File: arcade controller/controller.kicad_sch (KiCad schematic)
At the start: 21 parts, among them SW1 SW_DIP_x01, SW10 SW_DIP_x01, SW2 SW_DIP_x01, SW3 SW_DIP_x01, SW4 SW_DIP_x01, SW5 SW_DIP_x01, SW6 SW_DIP_x01, SW7 SW_DIP_x01, SW8 SW_DIP_x01, SW9 SW_DIP_x01

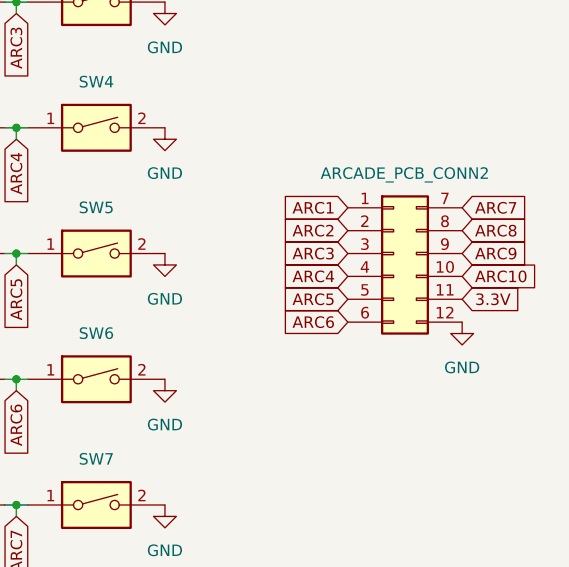
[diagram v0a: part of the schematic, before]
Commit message: updated controller with new connector
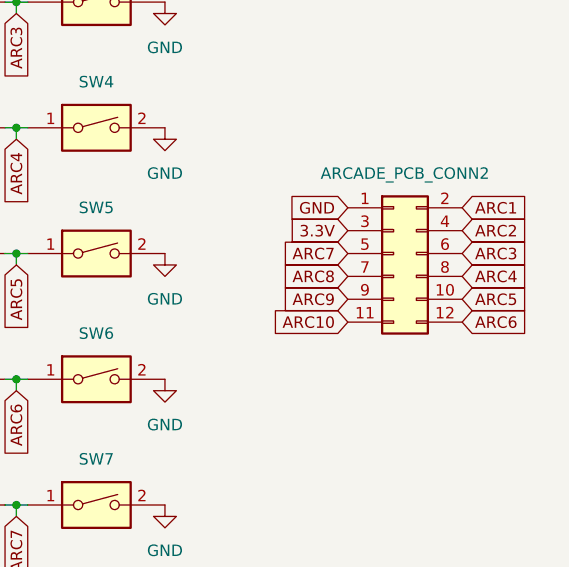
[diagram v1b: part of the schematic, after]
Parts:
- ARCADE_PCB_CONN2: value Conn_02x06_Top_Bottom -> Conn_02x06_Odd_Even; footprint Connector_Harwin:Harwin_Gecko-G125-FVX1205L0X_2x06_P1.25mm_Vertical -> Connector_PinHeader_2.54mm:PinHeader_2x06_P2.54mm_Vertical
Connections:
- net 3.3V: now also ARCADE_PCB_CONN2.3 (Pin_3); no longer ARCADE_PCB_CONN2.11 (Pin_11)
- net ARC1: now also ARCADE_PCB_CONN2.2 (Pin_2); no longer ARCADE_PCB_CONN2.1 (Pin_1)
- net ARC10: now also ARCADE_PCB_CONN2.11 (Pin_11); no longer ARCADE_PCB_CONN2.10 (Pin_10)
- net ARC2: now also ARCADE_PCB_CONN2.4 (Pin_4); no longer ARCADE_PCB_CONN2.2 (Pin_2)
- net ARC3: now also ARCADE_PCB_CONN2.6 (Pin_6); no longer ARCADE_PCB_CONN2.3 (Pin_3)
- net ARC4: now also ARCADE_PCB_CONN2.8 (Pin_8); no longer ARCADE_PCB_CONN2.4 (Pin_4)
- net ARC5: now also ARCADE_PCB_CONN2.10 (Pin_10); no longer ARCADE_PCB_CONN2.5 (Pin_5)
- net ARC6: now also ARCADE_PCB_CONN2.12 (Pin_12); no longer ARCADE_PCB_CONN2.6 (Pin_6)
- net ARC7: now also ARCADE_PCB_CONN2.5 (Pin_5); no longer ARCADE_PCB_CONN2.7 (Pin_7)
- net ARC8: now also ARCADE_PCB_CONN2.7 (Pin_7); no longer ARCADE_PCB_CONN2.8 (Pin_8)
- net GND: now also ARCADE_PCB_CONN2.1 (Pin_1); no longer ARCADE_PCB_CONN2.12 (Pin_12)

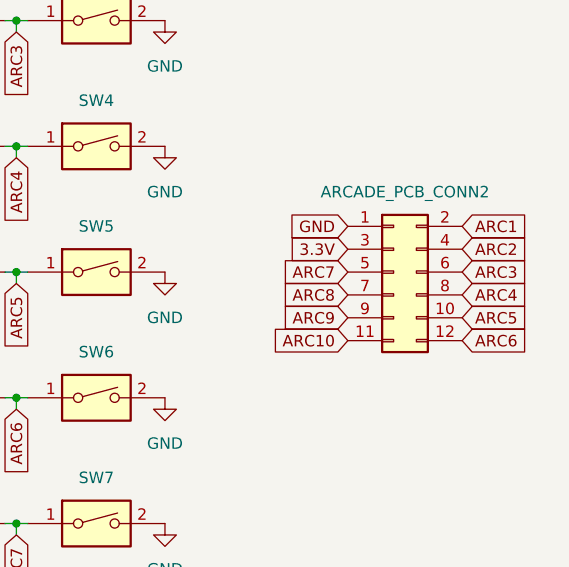
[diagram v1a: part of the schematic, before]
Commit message: update arcade controller
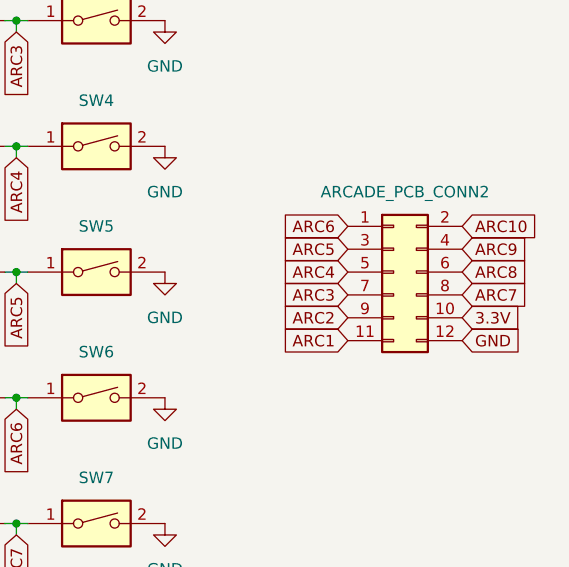
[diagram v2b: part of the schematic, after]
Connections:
- net 3.3V: now also ARCADE_PCB_CONN2.10 (Pin_10); no longer ARCADE_PCB_CONN2.3 (Pin_3)
- net ARC1: now also ARCADE_PCB_CONN2.11 (Pin_11); no longer ARCADE_PCB_CONN2.2 (Pin_2)
- net ARC10: now also ARCADE_PCB_CONN2.2 (Pin_2); no longer ARCADE_PCB_CONN2.11 (Pin_11)
- net ARC2: now also ARCADE_PCB_CONN2.9 (Pin_9); no longer ARCADE_PCB_CONN2.4 (Pin_4)
- net ARC3: now also ARCADE_PCB_CONN2.7 (Pin_7); no longer ARCADE_PCB_CONN2.6 (Pin_6)
- net ARC4: now also ARCADE_PCB_CONN2.5 (Pin_5); no longer ARCADE_PCB_CONN2.8 (Pin_8)
- net ARC5: now also ARCADE_PCB_CONN2.3 (Pin_3); no longer ARCADE_PCB_CONN2.10 (Pin_10)
- net ARC6: now also ARCADE_PCB_CONN2.1 (Pin_1); no longer ARCADE_PCB_CONN2.12 (Pin_12)
- net ARC7: now also ARCADE_PCB_CONN2.8 (Pin_8); no longer ARCADE_PCB_CONN2.5 (Pin_5)
- net ARC8: now also ARCADE_PCB_CONN2.6 (Pin_6); no longer ARCADE_PCB_CONN2.7 (Pin_7)
- net ARC9: now also ARCADE_PCB_CONN2.4 (Pin_4); no longer ARCADE_PCB_CONN2.9 (Pin_9)
- net GND: now also ARCADE_PCB_CONN2.12 (Pin_12); no longer ARCADE_PCB_CONN2.1 (Pin_1)
